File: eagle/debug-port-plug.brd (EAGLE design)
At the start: 9.8 x 15.8 mm, 1 part, among them J1 M50-3101045

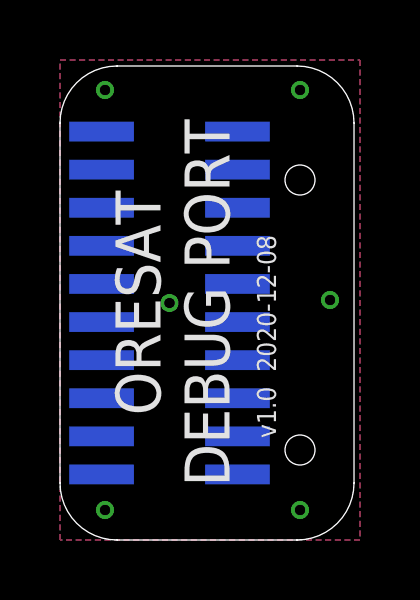
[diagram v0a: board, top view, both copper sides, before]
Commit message: v1.1 of the debug port plug. Perhaps it's not a great to short out literally every pin on the bus to ground? Maybe?
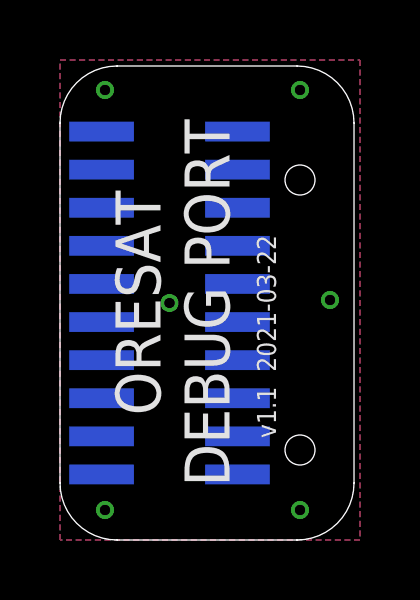
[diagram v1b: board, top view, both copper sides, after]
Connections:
- net GND: no longer J1.1, J1.10, J1.11, J1.12, J1.13, J1.17, J1.18, J1.2, J1.20, J1.3, J1.4, J1.5, J1.6, J1.7, J1.8, J1.9
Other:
- board text added: "v1.1 2021-03-22"
- board text removed: "v1.0 2020-12-08"
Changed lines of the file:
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@@
 <grid distance="0.1" unitdist="mm" unit="mm" style="lines" multiple="1" display="yes" altdistance="5" altunitdist="mil" altunit="mil"/>
 <layers>
-<layer number="1" name="Top" color="4" fill="1" visible="yes" active="yes"/>
+<layer number="1" name="Top" color="4" fill="1" visible="no" active="yes"/>
 <layer number="2" name="Route2" color="16" fill="1" visible="no" active="no"/>
 <layer number="3" name="Route3" color="17" fill="1" visible="no" active="no"/>
@@
 <layer number="19" name="Unrouted" color="6" fill="1" visible="yes" active="yes"/>
 <layer number="20" name="Dimension" color="24" fill="1" visible="yes" active="yes"/>
-<layer number="21" name="tPlace" color="7" fill="1" visible="yes" active="yes"/>
+<layer number="21" name="tPlace" color="7" fill="1" visible="no" active="yes"/>
 <layer number="22" name="bPlace" color="7" fill="1" visible="yes" active="yes"/>
-<layer number="23" name="tOrigins" color="15" fill="1" visible="yes" active="yes"/>
+<layer number="23" name="tOrigins" color="15" fill="1" visible="no" active="yes"/>
 <layer number="24" name="bOrigins" color="15" fill="1" visible="yes" active="yes"/>
 <layer number="25" name="tNames" color="7" fill="1" visible="no" active="yes"/>
@@
 <layer number="49" name="Reference" color="7" fill="1" visible="no" active="yes"/>
 <layer number="50" name="dxf" color="61" fill="1" visible="no" active="yes"/>
-<layer number="51" name="tDocu" color="7" fill="1" visible="yes" active="yes"/>
+<layer number="51" name="tDocu" color="7" fill="1" visible="no" active="yes"/>
 <layer number="52" name="bDocu" color="7" fill="1" visible="yes" active="yes"/>
 <layer number="53" name="tGND_GNDA" color="7" fill="9" visible="no" active="no"/>
@@
 <hole x="8" y="3" drill="1"/>
 <hole x="8" y="12" drill="1"/>
-<text x="7.2" y="3.4" size="0.635" layer="21" font="vector" ratio="20" rot="R90">v1.0  2020-12-08</text>
+<text x="7.2" y="3.4" size="0.635" layer="21" font="vector" ratio="20" rot="R90">v1.1  2021-03-22</text>
 <text x="2.6" y="7.9" size="1.5" layer="21" font="vector" ratio="15" rot="R90" align="center">ORESAT</text>
 </plain>
@@
 <via x="3.65" y="7.9" extent="1-16" drill="0.35"/>
 <via x="1.5" y="15" extent="1-16" drill="0.35"/>
-<contactref element="J1" pad="1"/>
-<contactref element="J1" pad="2"/>
-<contactref element="J1" pad="3"/>
-<contactref element="J1" pad="4"/>
-<contactref element="J1" pad="5"/>
-<contactref element="J1" pad="6"/>
-<contactref element="J1" pad="7"/>
-<contactref element="J1" pad="8"/>
-<contactref element="J1" pad="9"/>
-<contactref element="J1" pad="10"/>
-<contactref element="J1" pad="11"/>
-<contactref element="J1" pad="12"/>
-<contactref element="J1" pad="13"/>
 <contactref element="J1" pad="14"/>
 <contactref element="J1" pad="15"/>
+<contactref element="J1" pad="19"/>
 <contactref element="J1" pad="16"/>
-<contactref element="J1" pad="17"/>
-<contactref element="J1" pad="18"/>
-<contactref element="J1" pad="19"/>
-<contactref element="J1" pad="20"/>
 </signal>
 </signals>
